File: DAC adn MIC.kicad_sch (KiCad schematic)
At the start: 28 parts, among them J401 AudioJack2_Ground, J402 Conn_01x04_Pin, U401 CS43L22-CNZ, U402 IMP34DT05TR

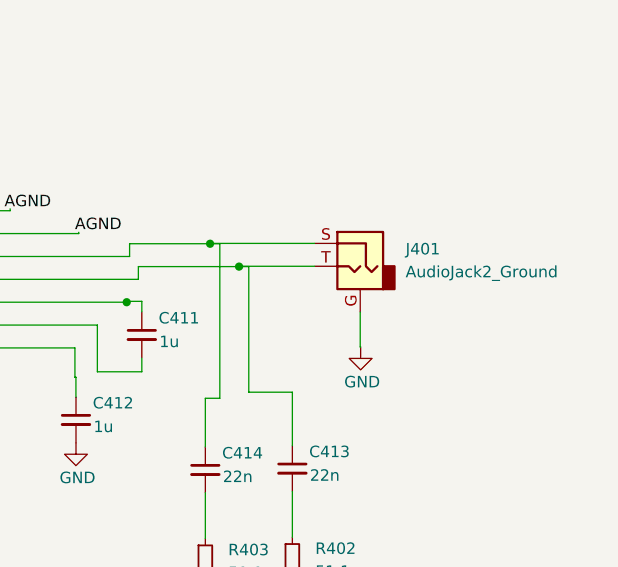
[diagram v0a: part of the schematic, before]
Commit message: ethernet, debugger and usb layouts re-designed
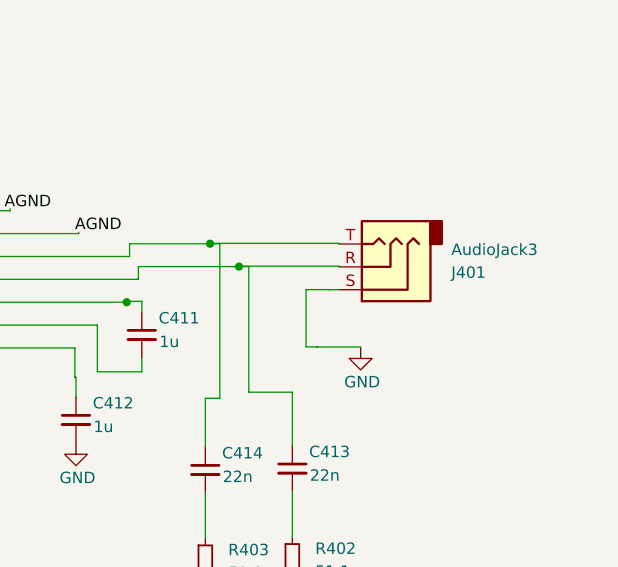
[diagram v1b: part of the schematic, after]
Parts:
- removed J401: AudioJack2_Ground, Connector_Audio:Jack_3.5mm_CUI_SJ1-3523N_Horizontal, symbol Connector_Audio:AudioJack2_Ground
- added J401: AudioJack3, Connector_Audio:Jack_3.5mm_CUI_SJ-3523-SMT_Horizontal, symbol Connector_Audio:AudioJack3
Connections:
- net GND: now also J401.S
- net at C414.1, U401.14 (HP/LINE_OUTB): now also J401.T
- net at C413.1, U401.15 (HP/LINE_OUTA): now also J401.R
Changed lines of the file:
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@@
 	(wire
 		(pts
-			(xy 234.8171 79.9206) (xy 246.4177 79.9206)
+			(xy 234.8171 79.9115) (xy 249.1411 79.9115)
 		)
 		(stroke
@@
 	(wire
 		(pts
-			(xy 234.8171 79.9206) (xy 234.8171 79.9573)
+			(xy 234.8171 79.9115) (xy 234.8171 79.9573)
 		)
 		(stroke
@@
 	(wire
 		(pts
+			(xy 246.7227 91.4188) (xy 246.7227 91.4315)
+		)
+		(stroke
+			(width 0)
+			(type default)
+		)
+	)
+	(wire
+		(pts
 			(xy 187.9333 41.7541) (xy 193.3528 41.7541)
 		)
@@
 	(wire
 		(pts
+			(xy 246.7227 91.4315) (xy 251.5428 91.4315)
+		)
+		(stroke
+			(width 0)
+			(type default)
+		)
+	)
+	(wire
+		(pts
 			(xy 158.8839 39.5682) (xy 153.688 39.5682)
 		)
@@
 	(wire
 		(pts
+			(xy 247.9927 85.0544) (xy 247.9927 85.0671)
+		)
+		(stroke
+			(width 0)
+			(type default)
+		)
+	)
+	(wire
+		(pts
 			(xy 227.2317 86.3577) (xy 225.5526 86.3577)
 		)
@@
 	(wire
 		(pts
+			(xy 249.1411 82.4515) (xy 249.1411 82.5271)
+		)
+		(stroke
+			(width 0)
+			(type default)
+		)
+	)
+	(wire
+		(pts
 			(xy 65.9404 88.7445) (xy 65.9404 88.7466)
 		)
@@
 	(wire
 		(pts
+			(xy 247.9927 85.0671) (xy 249.1411 85.0671)
+		)
+		(stroke
+			(width 0)
+			(type default)
+		)
+	)
+	(wire
+		(pts
 			(xy 171.3687 127.0946) (xy 171.3687 129.8015)
 		)
@@
 	(wire
 		(pts
-			(xy 251.4977 91.4315) (xy 251.5428 91.4315)
+			(xy 245.4865 91.4188) (xy 246.7227 91.4188)
 		)
 		(stroke
@@
 	(wire
 		(pts
-			(xy 251.4977 87.5406) (xy 251.4977 91.4315)
+			(xy 245.4865 85.0544) (xy 245.4865 91.4188)
 		)
 		(stroke
@@
 	(wire
 		(pts
+			(xy 247.9927 85.0544) (xy 245.4865 85.0544)
+		)
+		(stroke
+			(width 0)
+			(type default)
+		)
+	)
+	(wire
+		(pts
 			(xy 165.5338 76.2946) (xy 190.6556 76.2946)
 		)
@@
 	(wire
 		(pts
+			(xy 249.1411 79.9115) (xy 249.1411 79.9871)
+		)
+		(stroke
+			(width 0)
+			(type default)
+		)
+	)
+	(wire
+		(pts
 			(xy 121.1567 48.1946) (xy 131.539 48.1946)
 		)
@@
 	(wire
 		(pts
-			(xy 238.035 82.4606) (xy 246.4177 82.4606)
+			(xy 238.035 82.4515) (xy 249.1411 82.4515)
 		)
 		(stroke
@@
 	(wire
 		(pts
-			(xy 238.035 82.4606) (xy 238.035 82.4973)
+			(xy 238.035 82.4515) (xy 238.035 82.4973)
 		)
 		(stroke
@@
 	)
 	(symbol
-		(lib_id "Connector_Audio:AudioJack2_Ground")
-		(at 251.4977 82.4606 0)
-		(mirror y)
-		(unit 1)
-		(exclude_from_sim no)
-		(in_bom yes)
-		(on_board yes)
-		(dnp no)
-		(fields_autoplaced yes)
-		(property "Reference" "J401"
-			(at 256.54 80.5555 0)
-			(effects
-				(font
-					(size 1.27 1.27)
-				)
-				(justify right)
-			)
-		)
-		(property "Value" "AudioJack2_Ground"
-			(at 256.54 83.0955 0)
-			(effects
-				(font
-					(size 1.27 1.27)
-				)
-				(justify right)
-			)
-		)
-		(property "Footprint" "Connector_Audio:Jack_3.5mm_CUI_SJ1-3523N_Horizontal"
-			(at 251.4977 82.4606 0)
-			(effects
-				(font
-					(size 1.27 1.27)
-				)
-				(hide yes)
-			)
-		)
-		(property "Datasheet" "~"
-			(at 251.4977 82.4606 0)
-			(effects
-				(font
-					(size 1.27 1.27)
-				)
-				(hide yes)
-			)
-		)
-		(property "Description" "Audio Jack, 2 Poles (Mono / TS), Grounded Sleeve"
-			(at 251.4977 82.4606 0)
-			(effects
-				(font
-					(size 1.27 1.27)
-				)
-				(hide yes)
-			)
-		)
-		(pin "G"
-		)
-		(pin "T"
-		)
-		(pin "S"
-		)
-		(instances
-			(project ""
-				(path "/8a424437-6f3e-424c-a786-3b8b285eee60/087b0ea2-dd54-459d-a3b3-b58577c2dfaa"
-					(reference "J401")
-					(unit 1)
-				)
-			)
-		)
-	)
-	(symbol
 		(lib_id "dk_Ferrite-Beads-and-Chips:BLM18HE152SN1D")
 		(at 169.6383 29.6176 0)
@@
 					(unit 1)
 				)
+			)
+		)
+	)
+	(symbol
+		(lib_id "Connector_Audio:AudioJack3")
+		(at 254.2211 82.5271 180)
+		(unit 1)
+		(exclude_from_sim no)
+		(in_bom yes)
+		(on_board yes)
+		(dnp no)
+		(property "Reference" "J401"
+			(at 261.6149 83.1622 0)
+			(effects
+				(font
+					(size 1.27 1.27)
+				)
+				(justify right)
+			)
+		)
+		(property "Value" "AudioJack3"
+			(at 261.6149 80.6222 0)
+			(effects
+				(font
+					(size 1.27 1.27)
+				)
+				(justify right)
+			)
+		)
+		(property "Footprint" "Connector_Audio:Jack_3.5mm_CUI_SJ-3523-SMT_Horizontal"
+			(at 254.2211 82.5271 0)
+			(effects
+				(font
+					(size 1.27 1.27)
+				)
+				(hide yes)
+			)
+		)
+		(property "Datasheet" "~"
+			(at 254.2211 82.5271 0)
+			(effects
+				(font
+					(size 1.27 1.27)
+				)
+				(hide yes)
+			)
+		)
+		(property "Description" "Audio Jack, 3 Poles (Stereo / TRS)"
+			(at 254.2211 82.5271 0)
+			(effects
+				(font
+					(size 1.27 1.27)
+				)
+				(hide yes)
+			)
+		)
+		(pin "T"
+		)
+		(pin "S"
+		)
+		(pin "R"
+		)
+		(instances
+			(project "mixed signal board project"
+				(path "/8a424437-6f3e-424c-a786-3b8b285eee60/087b0ea2-dd54-459d-a3b3-b58577c2dfaa"
+					(reference "J401")
+					(unit 1)
+				)

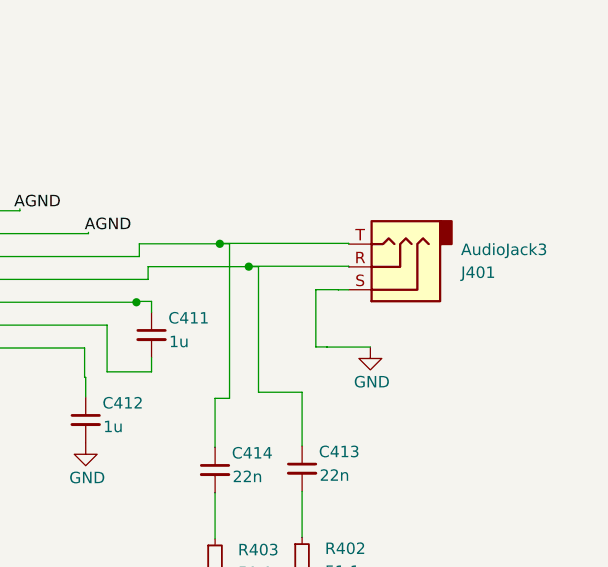
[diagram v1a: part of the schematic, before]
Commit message: MIC footprint changed, all blocks routed internally, next step is route all to the MCU
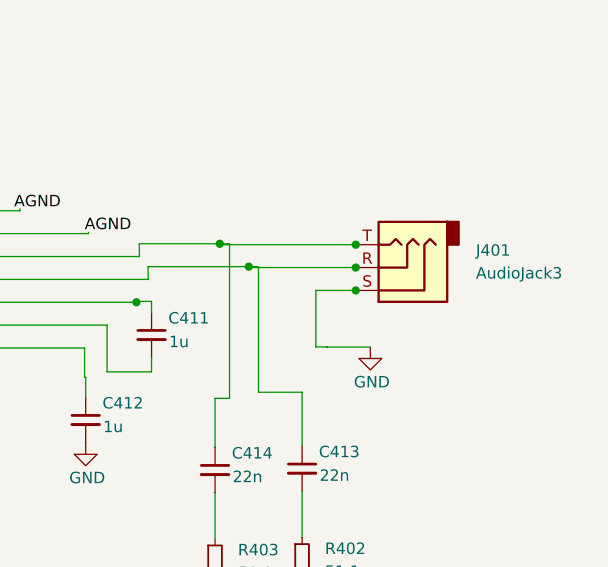
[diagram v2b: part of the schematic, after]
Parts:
- J401: footprint Connector_Audio:Jack_3.5mm_CUI_SJ-3523-SMT_Horizontal -> Connector_Audio:Jack_3.5mm_Lumberg_1503_02_Horizontal
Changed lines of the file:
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@@
 	)
 	(junction
+		(at 249.9241 85.1383)
+		(diameter 0)
+		(color 0 0 0 0)
+	)
+	(junction
 		(at 65.9404 75.4956)
 		(diameter 0)
@@
 	)
 	(junction
+		(at 249.9241 82.5983)
+		(diameter 0)
+		(color 0 0 0 0)
+	)
+	(junction
 		(at 158.8839 29.6176)
 		(diameter 0)
@@
 		(color 0 0 0 0)
 	)
+	(junction
+		(at 249.9241 80.0583)
+		(diameter 0)
+		(color 0 0 0 0)
+	)
 	(no_connect
 		(at 124.8938 83.9146)
@@
 	(wire
 		(pts
-			(xy 234.8171 79.9115) (xy 249.1411 79.9115)
+			(xy 234.8171 80.0583) (xy 249.9241 80.0583)
 		)
 		(stroke
@@
 	(wire
 		(pts
-			(xy 234.8171 79.9115) (xy 234.8171 79.9573)
+			(xy 234.8171 80.0583) (xy 234.8171 79.9573)
 		)
 		(stroke
@@
 	(wire
 		(pts
-			(xy 247.9927 85.0544) (xy 247.9927 85.0671)
+			(xy 249.9241 85.1383) (xy 249.9241 85.0671)
 		)
 		(stroke
@@
 	(wire
 		(pts
-			(xy 249.1411 82.4515) (xy 249.1411 82.5271)
+			(xy 249.9241 82.5983) (xy 249.9241 82.5271)
 		)
 		(stroke
@@
 	(wire
 		(pts
-			(xy 247.9927 85.0671) (xy 249.1411 85.0671)
-		)
-		(stroke
-			(width 0)
-			(type default)
-		)
-	)
-	(wire
-		(pts
 			(xy 171.3687 127.0946) (xy 171.3687 129.8015)
 		)
@@
 	(wire
 		(pts
-			(xy 245.4865 85.0544) (xy 245.4865 91.4188)
+			(xy 245.4865 85.1383) (xy 245.4865 91.4188)
 		)
 		(stroke
@@
 	(wire
 		(pts
-			(xy 247.9927 85.0544) (xy 245.4865 85.0544)
+			(xy 249.9241 85.1383) (xy 245.4865 85.1383)
 		)
 		(stroke
@@
 	(wire
 		(pts
-			(xy 249.1411 79.9115) (xy 249.1411 79.9871)
+			(xy 249.9241 80.0583) (xy 249.9241 79.9871)
 		)
 		(stroke
@@
 	(wire
 		(pts
-			(xy 238.035 82.4515) (xy 249.1411 82.4515)
+			(xy 238.035 82.5983) (xy 249.9241 82.5983)
 		)
 		(stroke
@@
 	(wire
 		(pts
-			(xy 238.035 82.4515) (xy 238.035 82.4973)
+			(xy 238.035 82.5983) (xy 238.035 82.4973)
 		)
 		(stroke
@@
 	)
 	(symbol
+		(lib_id "Connector_Audio:AudioJack3")
+		(at 255.0041 82.5983 180)
+		(unit 1)
+		(exclude_from_sim no)
+		(in_bom yes)
+		(on_board yes)
+		(dnp no)
+		(fields_autoplaced yes)
+		(property "Reference" "J401"
+			(at 263.27 80.6932 0)
+			(effects
+				(font
+					(size 1.27 1.27)
+				)
+				(justify right)
+			)
+		)
+		(property "Value" "AudioJack3"
+			(at 263.27 83.2332 0)
+			(effects
+				(font
+					(size 1.27 1.27)
+				)
+				(justify right)
+			)
+		)
+		(property "Footprint" "Connector_Audio:Jack_3.5mm_Lumberg_1503_02_Horizontal"
+			(at 255.0041 82.5983 0)
+			(effects
+				(font
+					(size 1.27 1.27)
+				)
+				(hide yes)
+			)
+		)
+		(property "Datasheet" "~"
+			(at 255.0041 82.5983 0)
+			(effects
+				(font
+					(size 1.27 1.27)
+				)
+				(hide yes)
+			)
+		)
+		(property "Description" "Audio Jack, 3 Poles (Stereo / TRS)"
+			(at 255.0041 82.5983 0)
+			(effects
+				(font
+					(size 1.27 1.27)
+				)
+				(hide yes)
+			)
+		)
+		(pin "S"
+		)
+		(pin "T"
+		)
+		(pin "R"
+		)
+		(instances
+			(project ""
+				(path "/8a424437-6f3e-424c-a786-3b8b285eee60/087b0ea2-dd54-459d-a3b3-b58577c2dfaa"
+					(reference "J401")
+					(unit 1)
+				)
+			)
+		)
+	)
+	(symbol
 		(lib_id "power:GND")
 		(at 240.1476 123.8252 0)
@@
 					(unit 1)
 				)
-			)
-		)
-	)
-	(symbol
-		(lib_id "Connector_Audio:AudioJack3")
-		(at 254.2211 82.5271 180)
-		(unit 1)
-		(exclude_from_sim no)
-		(in_bom yes)
-		(on_board yes)
-		(dnp no)
-		(property "Reference" "J401"
-			(at 261.6149 83.1622 0)
-			(effects
-				(font
-					(size 1.27 1.27)
-				)
-				(justify right)
-			)
-		)
-		(property "Value" "AudioJack3"
-			(at 261.6149 80.6222 0)
-			(effects
-				(font
-					(size 1.27 1.27)
-				)
-				(justify right)
-			)
-		)
-		(property "Footprint" "Connector_Audio:Jack_3.5mm_CUI_SJ-3523-SMT_Horizontal"
-			(at 254.2211 82.5271 0)
-			(effects
-				(font
-					(size 1.27 1.27)
-				)
-				(hide yes)
-			)
-		)
-		(property "Datasheet" "~"
-			(at 254.2211 82.5271 0)
-			(effects
-				(font
-					(size 1.27 1.27)
-				)
-				(hide yes)
-			)
-		)
-		(property "Description" "Audio Jack, 3 Poles (Stereo / TRS)"
-			(at 254.2211 82.5271 0)
-			(effects
-				(font
-					(size 1.27 1.27)
-				)
-				(hide yes)
-			)
-		)
-		(pin "T"
-		)
-		(pin "S"
-		)
-		(pin "R"
-		)
-		(instances
-			(project "mixed signal board project"
-				(path "/8a424437-6f3e-424c-a786-3b8b285eee60/087b0ea2-dd54-459d-a3b3-b58577c2dfaa"
-					(reference "J401")
-					(unit 1)
-				)

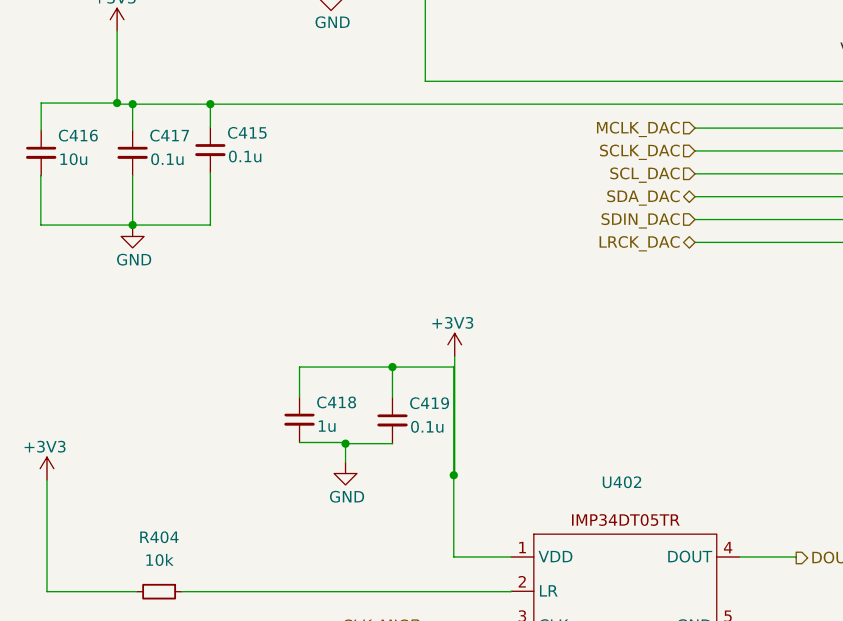
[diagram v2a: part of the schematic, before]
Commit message: some design failures reviewed(MIC VDD is 1V8, Motor Drivers' pull-up to DVDD pin, I2C net fixed). Routing mostly done.
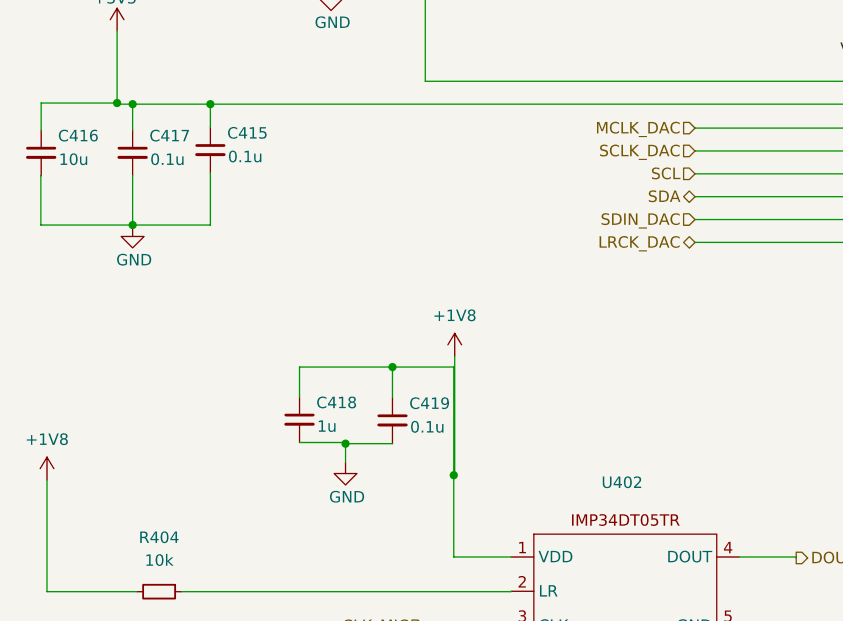
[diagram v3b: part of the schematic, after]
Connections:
- net +1V8: now also C418.1, C419.1, R404.2, U402.1 (VDD)
- net +3V3: no longer C418.1, C419.1, R404.2, U402.1 (VDD)
- net SCL_DAC renamed SCL
- net SDA_DAC renamed SDA
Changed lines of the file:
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@@
 		)
 	)
-	(hierarchical_label "SDA_DAC"
+	(hierarchical_label "SDA"
 		(shape bidirectional)
 		(at 106.3783 111.9758 180)
@@
 		)
 	)
-	(hierarchical_label "SCL_DAC"
+	(hierarchical_label "SCL"
 		(shape input)
 		(at 106.3783 109.4358 180)
@@
 	)
 	(symbol
+		(lib_id "power:+2V5")
+		(at 34.3744 143.4649 0)
+		(unit 1)
+		(exclude_from_sim no)
+		(in_bom yes)
+		(on_board yes)
+		(dnp no)
+		(fields_autoplaced yes)
+		(property "Reference" "#PWR0505"
+			(at 34.3744 147.2749 0)
+			(effects
+				(font
+					(size 1.27 1.27)
+				)
+				(hide yes)
+			)
+		)
+		(property "Value" "+1V8"
+			(at 34.3744 138.9664 0)
+			(effects
+				(font
+					(size 1.27 1.27)
+				)
+			)
+		)
+		(property "Footprint" ""
+			(at 34.3744 143.4649 0)
+			(effects
+				(font
+					(size 1.27 1.27)
+				)
+				(hide yes)
+			)
+		)
+		(property "Datasheet" ""
+			(at 34.3744 143.4649 0)
+			(effects
+				(font
+					(size 1.27 1.27)
+				)
+				(hide yes)
+			)
+		)
+		(property "Description" "Power symbol creates a global label with name \"+2V5\""
+			(at 34.3744 143.4649 0)
+			(effects
+				(font
+					(size 1.27 1.27)
+				)
+				(hide yes)
+			)
+		)
+		(pin "1"
+		)
+		(instances
+			(project "mixed signal board project"
+				(path "/8a424437-6f3e-424c-a786-3b8b285eee60/087b0ea2-dd54-459d-a3b3-b58577c2dfaa"
+					(reference "#PWR0505")
+					(unit 1)
+				)
+			)
+		)
+	)
+	(symbol
 		(lib_id "Device:C_Small")
 		(at 187.9333 35.3189 0)
@@
 	)
 	(symbol
-		(lib_id "power:+3V3")
-		(at 34.3744 143.4649 0)
-		(unit 1)
-		(exclude_from_sim no)
-		(in_bom yes)
-		(on_board yes)
-		(dnp no)
-		(property "Reference" "#PWR0828"
-			(at 34.3744 147.2749 0)
-			(effects
-				(font
-					(size 1.27 1.27)
-				)
-				(hide yes)
-			)
-		)
-		(property "Value" "+3V3"
-			(at 34.1366 139.8024 0)
-			(effects
-				(font
-					(size 1.27 1.27)
-				)
-			)
-		)
-		(property "Footprint" ""
-			(at 34.3744 143.4649 0)
-			(effects
-				(font
-					(size 1.27 1.27)
-				)
-				(hide yes)
-			)
-		)
-		(property "Datasheet" ""
-			(at 34.3744 143.4649 0)
-			(effects
-				(font
-					(size 1.27 1.27)
-				)
-				(hide yes)
-			)
-		)
-		(property "Description" "Power symbol creates a global label with name \"+3V3\""
-			(at 34.3744 143.4649 0)
-			(effects
-				(font
-					(size 1.27 1.27)
-				)
-				(hide yes)
-			)
-		)
-		(pin "1"
-		)
-		(instances
-			(project "mixed signal board project"
-				(path "/8a424437-6f3e-424c-a786-3b8b285eee60/087b0ea2-dd54-459d-a3b3-b58577c2dfaa"
-					(reference "#PWR0828")
-					(unit 1)
-				)
-			)
-		)
-	)
-	(symbol
 		(lib_id "Device:R_Small")
 		(at 46.8323 155.8636 270)
@@
 	)
 	(symbol
+		(lib_id "power:+2V5")
+		(at 79.6777 129.7045 0)
+		(unit 1)
+		(exclude_from_sim no)
+		(in_bom yes)
+		(on_board yes)
+		(dnp no)
+		(fields_autoplaced yes)
+		(property "Reference" "#PWR0504"
+			(at 79.6777 133.5145 0)
+			(effects
+				(font
+					(size 1.27 1.27)
+				)
+				(hide yes)
+			)
+		)
+		(property "Value" "+1V8"
+			(at 79.6777 125.206 0)
+			(effects
+				(font
+					(size 1.27 1.27)
+				)
+			)
+		)
+		(property "Footprint" ""
+			(at 79.6777 129.7045 0)
+			(effects
+				(font
+					(size 1.27 1.27)
+				)
+				(hide yes)
+			)
+		)
+		(property "Datasheet" ""
+			(at 79.6777 129.7045 0)
+			(effects
+				(font
+					(size 1.27 1.27)
+				)
+				(hide yes)
+			)
+		)
+		(property "Description" "Power symbol creates a global label with name \"+2V5\""
+			(at 79.6777 129.7045 0)
+			(effects
+				(font
+					(size 1.27 1.27)
+				)
+				(hide yes)
+			)
+		)
+		(pin "1"
+		)
+		(instances
+			(project "mixed signal board project"
+				(path "/8a424437-6f3e-424c-a786-3b8b285eee60/087b0ea2-dd54-459d-a3b3-b58577c2dfaa"
+					(reference "#PWR0504")
+					(unit 1)
+				)
+			)
+		)
+	)
+	(symbol
 		(lib_id "power:GND")
 		(at 67.5455 141.4658 0)
@@
 					(unit 1)
 				)
-			)
-		)
-	)
-	(symbol
-		(lib_id "power:+3V3")
-		(at 79.6777 129.7045 0)
-		(unit 1)
-		(exclude_from_sim no)
-		(in_bom yes)
-		(on_board yes)
-		(dnp no)
-		(property "Reference" "#PWR0827"
-			(at 79.6777 133.5145 0)
-			(effects
-				(font
-					(size 1.27 1.27)
-				)
-				(hide yes)
-			)
-		)
-		(property "Value" "+3V3"
-			(at 79.4399 126.042 0)
-			(effects
-				(font
-					(size 1.27 1.27)
-				)
-			)
-		)
-		(property "Footprint" ""
-			(at 79.6777 129.7045 0)
-			(effects
-				(font
-					(size 1.27 1.27)
-				)
-				(hide yes)
-			)
-		)
-		(property "Datasheet" ""
-			(at 79.6777 129.7045 0)
-			(effects
-				(font
-					(size 1.27 1.27)
-				)
-				(hide yes)
-			)
-		)
-		(property "Description" "Power symbol creates a global label with name \"+3V3\""
-			(at 79.6777 129.7045 0)
-			(effects
-				(font
-					(size 1.27 1.27)
-				)
-				(hide yes)
-			)
-		)
-		(pin "1"
-		)
-		(instances
-			(project "mixed signal board project"
-				(path "/8a424437-6f3e-424c-a786-3b8b285eee60/087b0ea2-dd54-459d-a3b3-b58577c2dfaa"
-					(reference "#PWR0827")
-					(unit 1)
-				)

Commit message: some additions
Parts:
- renumbered C406 to C?, C414 to C?, C417 to C?, C402 to C?, C411 to C?, C401 to C?, C413 to C?, C415 to C?, C410 to C?, C419 to C?, C407 to C?, C404 to C?, C412 to C?, C409 to C?, C408 to C?, C416 to C?, C405 to C?, C403 to C?, C418 to C?, FB401 to FB?, J401 to J?, J402 to J?, R404 to R?, R403 to R?, R402 to R?, R401 to R?, U402 to U?, U401 to U?
